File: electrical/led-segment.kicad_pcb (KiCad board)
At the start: 2 copper layers, 53.8 x 97.5 mm, 52 parts, among them P1 CONN_3, P2 CONN_20, P3 CONN_3, P4 CONN_20, Q1 FDV301N, Q2 FDV301N, Q3 FDV301N, Q4 FDV301N, Q5 FDV301N, Q6 FDV301N, U1 74164

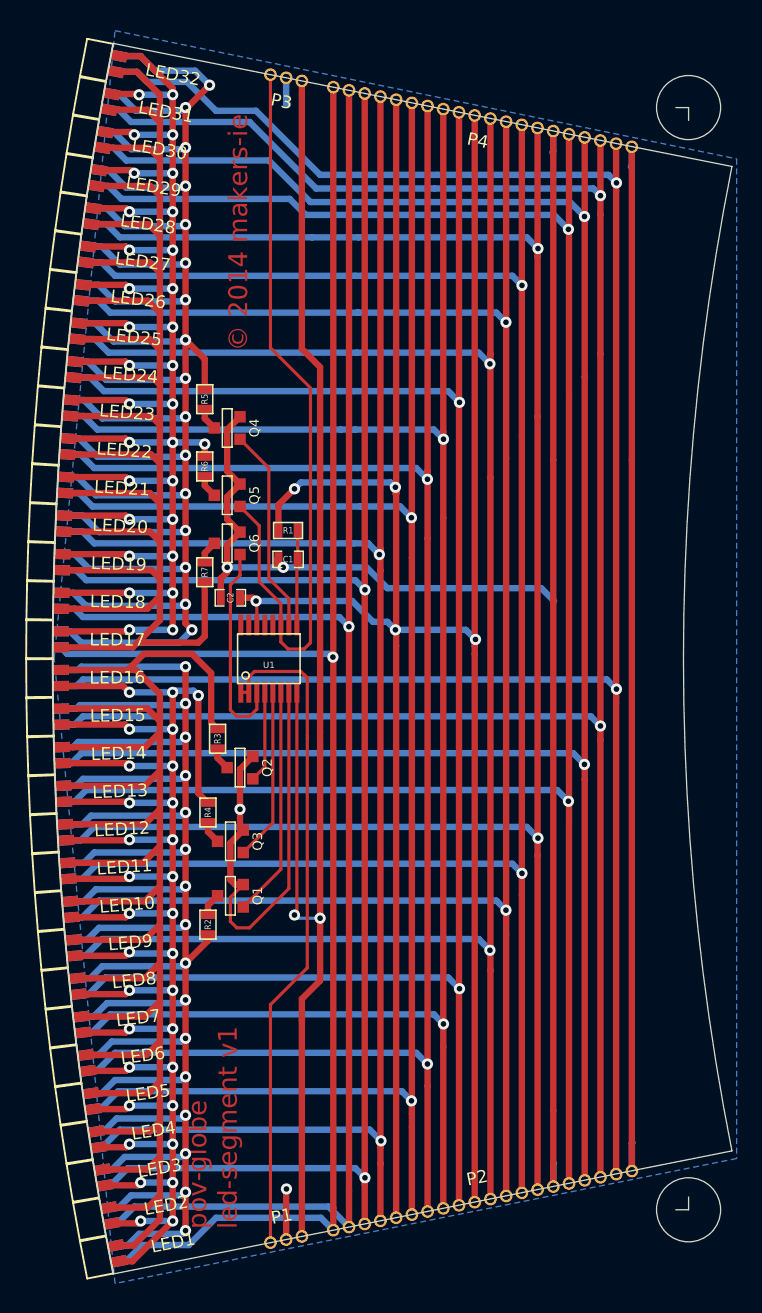
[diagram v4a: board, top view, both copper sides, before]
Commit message: Move led-segment text to silk screen. Add 50x100 mm edge cut.
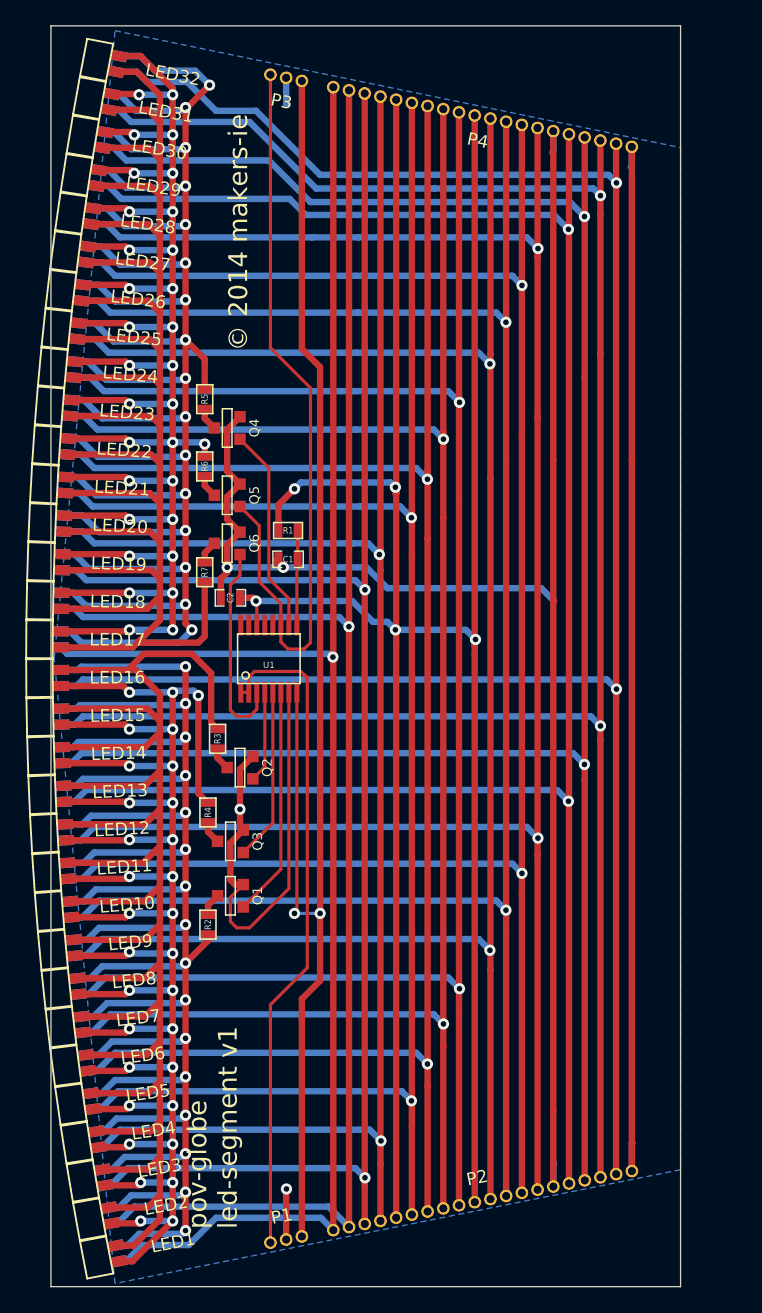
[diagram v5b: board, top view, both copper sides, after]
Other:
- board size 53.8 x 97.5 mm -> 49.9 x 99.9 mm
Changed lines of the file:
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@@
     (area 56.122313 113.115159 309.626001 223.399712)
     (thickness 1.6)
-    (drawings 12)
-    (tracks 1014)
+    (drawings 10)
+    (tracks 1013)
     (zones 0)
     (modules 52)
@@
     (22 B.Mask user)
     (23 F.Mask user)
+    (26 Eco1.User user)
     (28 Edge.Cuts user)
   )
   (setup
-    (last_trace_width 0.508)
+    (last_trace_width 0.254)
     (user_trace_width 0.254)
     (trace_clearance 0.2286)
@@
     (zone_45_only no)
     (trace_min 0.254)
-    (segment_width 0.2)
+    (segment_width 0.1)
     (edge_width 0.1)
     (via_size 0.889)
@@
     (visible_elements 7FFFFFFF)
     (pcbplotparams
-      (layerselection 32769)
-      (usegerberextensions false)
+      (layerselection 283148289)
+      (usegerberextensions true)
       (excludeedgelayer true)
       (linewidth 0.150000)
-      (plotframeref true)
+      (plotframeref false)
       (viasonmask false)
       (mode 1)
@@
       (plotinvisibletext false)
       (padsonsilk false)
-      (subtractmaskfromsilk false)
-      (outputformat 2)
+      (subtractmaskfromsilk true)
+      (outputformat 1)
       (mirror false)
       (drillshape 0)
@@
     )
   )
-  (gr_text "pov-globe\nled-segment v1" (at 72.263 213.36 90) (layer F.Cu)
+  (gr_line (start 109.347 217.932) (end 59.436 217.932) (angle 90) (layer Edge.Cuts) (width 0.1))
+  (gr_line (start 109.347 117.983) (end 109.347 217.932) (angle 90) (layer Edge.Cuts) (width 0.1))
+  (gr_line (start 59.436 117.983) (end 109.347 117.983) (angle 90) (layer Edge.Cuts) (width 0.1))
+  (gr_line (start 59.436 217.932) (end 59.436 117.983) (angle 90) (layer Edge.Cuts) (width 0.1))
+  (gr_text "pov-globe\nled-segment v1" (at 72.263 213.36 90) (layer F.SilkS)
     (effects (font (size 1.5 1.5) (thickness 0.3)) (justify left))
   )
-  (gr_text "© 2014 makers-ie" (at 74.295 134.366 90) (layer F.Cu)
+  (gr_text "© 2014 makers-ie" (at 74.295 134.366 90) (layer F.SilkS)
     (effects (font (size 1.5 1.5) (thickness 0.3)))
   )
-  (gr_circle (center 109.982 211.836) (end 109.982 209.296) (layer Edge.Cuts) (width 0.1))
-  (gr_circle (center 109.982 124.46) (end 109.982 127) (layer Edge.Cuts) (width 0.1))
-  (gr_line (start 109.982 124.46) (end 108.966 124.46) (angle 90) (layer Edge.Cuts) (width 0.1))
-  (gr_line (start 109.982 125.476) (end 109.982 124.46) (angle 90) (layer Edge.Cuts) (width 0.1))
-  (gr_line (start 109.982 211.836) (end 109.982 210.82) (angle 90) (layer Edge.Cuts) (width 0.1))
-  (gr_line (start 108.966 211.836) (end 109.982 211.836) (angle 90) (layer Edge.Cuts) (width 0.1))
-  (gr_line (start 64.37968 119.375419) (end 113.418944 129.129936) (layer Edge.Cuts) (width 0.1))
-  (gr_arc (start 309.576 168.148) (end 64.37968 216.920581) (angle 22.5) (layer Edge.Cuts) (width 0.1))
-  (gr_line (start 64.37968 216.920581) (end 113.418944 207.166064) (layer Edge.Cuts) (width 0.1))
-  (gr_arc (start 309.576 168.148) (end 113.418944 207.166064) (angle 22.5) (layer Edge.Cuts) (width 0.1))
+  (gr_line (start 64.37968 119.375419) (end 113.418944 129.129936) (layer Eco1.User) (width 0.1))
+  (gr_arc (start 309.576 168.148) (end 64.37968 216.920581) (angle 22.5) (layer Eco1.User) (width 0.1))
+  (gr_line (start 64.37968 216.920581) (end 113.418944 207.166064) (layer Eco1.User) (width 0.1))
+  (gr_arc (start 309.576 168.148) (end 113.418944 207.166064) (angle 22.5) (layer Eco1.User) (width 0.1))
   (segment (start 86.741 165.862) (end 92.329 165.862) (width 0.508) (layer B.Cu) (net 1))
   (segment (start 93.091 166.624) (end 93.028418 166.624) (width 0.508) (layer F.Cu) (net 1))
@@
   (segment (start 71.882 188.468) (end 71.882 187.706) (width 0.508) (layer F.Cu) (net 38))
   (segment (start 71.882 187.706) (end 72.644 186.944) (width 0.508) (layer F.Cu) (net 38))
+  (segment (start 78.74 188.341) (end 80.772 188.341) (width 0.254) (layer B.Cu) (net 39))
+  (segment (start 78.9305 170.815) (end 78.9305 188.1505) (width 0.254) (layer F.Cu) (net 39))
+  (via (at 80.772 188.341) (size 0.889) (layers F.Cu B.Cu) (net 39))
+  (via (at 78.74 188.341) (size 0.889) (layers F.Cu B.Cu) (net 39))
+  (segment (start 78.9305 188.1505) (end 78.74 188.341) (width 0.254) (layer F.Cu) (net 39))
   (segment (start 79.327279 196.770721) (end 79.327279 195.119721) (width 0.508) (layer F.Cu) (net 39))
-  (segment (start 80.772 188.722) (end 80.772 193.675) (width 0.508) (layer F.Cu) (net 39))
+  (segment (start 80.772 188.341) (end 80.772 193.675) (width 0.508) (layer F.Cu) (net 39))
   (segment (start 79.327279 196.85) (end 79.327279 196.770721) (width 0.508) (layer F.Cu) (net 39))
   (segment (start 79.327279 213.949578) (end 79.327279 196.85) (width 0.508) (layer F.Cu) (net 39))
   (segment (start 79.327279 195.119721) (end 80.772 193.675) (width 0.508) (layer F.Cu) (net 39))
   (segment (start 79.326848 123.444) (end 79.326848 143.588848) (width 0.508) (layer F.Cu) (net 39))
-  (segment (start 80.772 173.99) (end 80.772 188.722) (width 0.508) (layer F.Cu) (net 39))
+  (segment (start 80.772 173.99) (end 80.772 188.341) (width 0.508) (layer F.Cu) (net 39))
   (segment (start 80.772 145.034) (end 80.772 173.99) (width 0.508) (layer F.Cu) (net 39))
   (segment (start 79.326848 122.348596) (end 79.326848 123.444) (width 0.508) (layer F.Cu) (net 39))
   (segment (start 79.326848 143.588848) (end 80.772 145.034) (width 0.508) (layer F.Cu) (net 39))
-  (segment (start 78.9305 170.815) (end 78.9305 188.2775) (width 0.254) (layer F.Cu) (net 39))
-  (via (at 80.772 188.722) (size 0.889) (layers F.Cu B.Cu) (net 39))
-  (segment (start 78.994 188.722) (end 80.772 188.722) (width 0.254) (layer B.Cu) (net 39))
-  (segment (start 78.74 188.468) (end 78.994 188.722) (width 0.254) (layer B.Cu) (net 39))
-  (via (at 78.74 188.468) (size 0.889) (layers F.Cu B.Cu) (net 39))
-  (segment (start 78.9305 188.2775) (end 78.74 188.468) (width 0.254) (layer F.Cu) (net 39))
   (zone (net 24) (net_name GND) (layer B.Cu) (hatch edge 0.508)
     (connect_pads (clearance 0.508))
@@
     (polygon
       (pts
-        (xy 113.792 207.772) (xy 64.516 217.678) (xy 59.69 168.148) (xy 64.516 118.364) (xy 113.792 128.524)
-        (xy 113.792 207.772)
+        (xy 64.516 217.678) (xy 59.69 168.148) (xy 64.516 118.364) (xy 109.347 127.635) (xy 109.347 208.661)
       )
     )

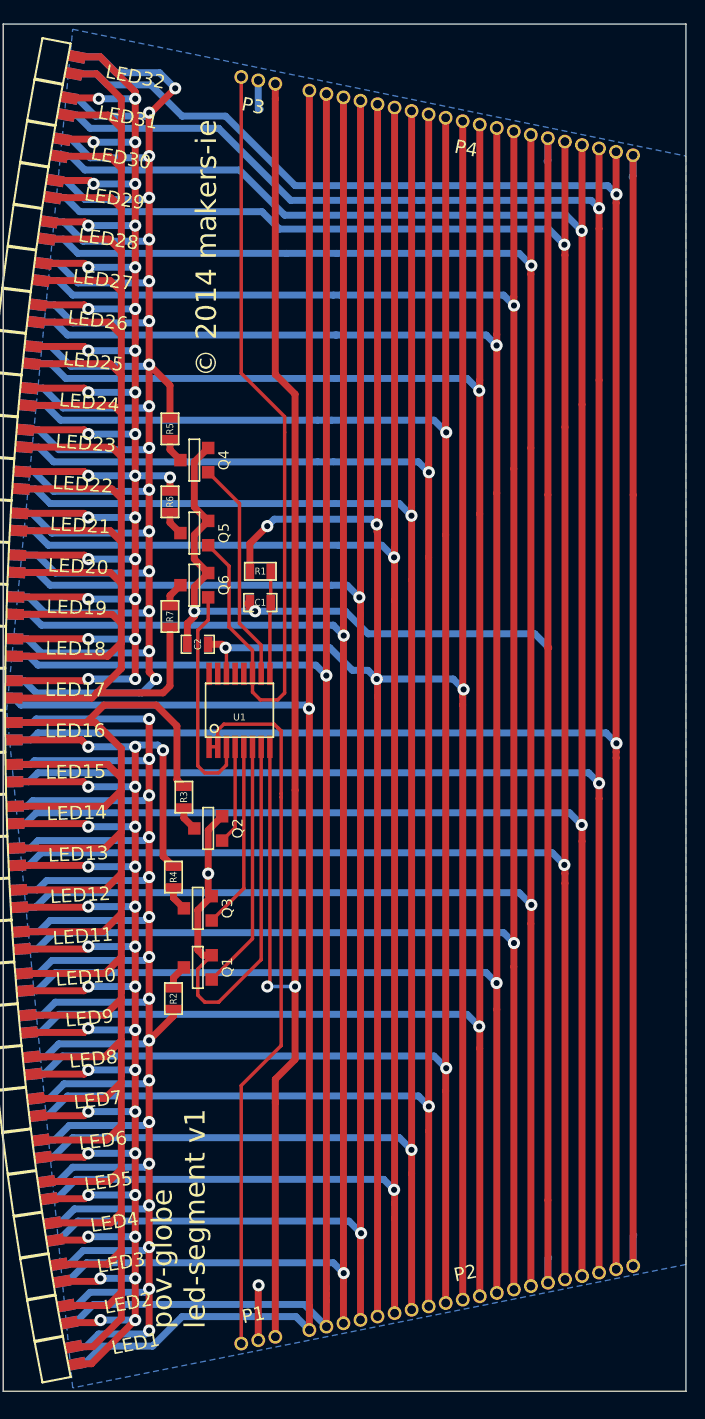
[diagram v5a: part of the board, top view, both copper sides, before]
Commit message: Increase all vias to 36/20 mil mil.
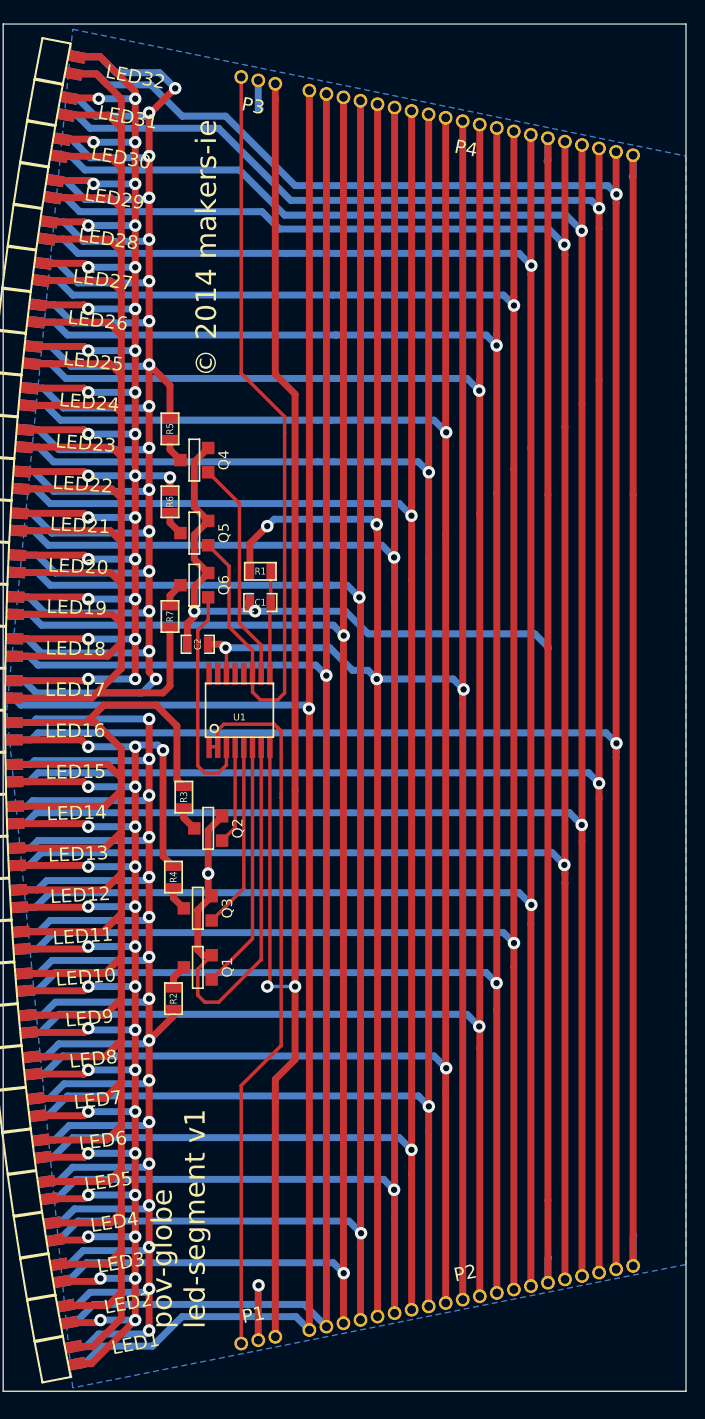
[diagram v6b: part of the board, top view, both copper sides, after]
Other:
- net class Default: via_dia 0.889 -> 0.9144; via_drill 0.635 -> 0.508
- net class signal: via_dia 0.889 -> 0.9144; via_drill 0.635 -> 0.508
- rule via_min_size: 0.889 -> 0.9144
